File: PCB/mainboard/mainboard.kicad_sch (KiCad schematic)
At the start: 42 parts

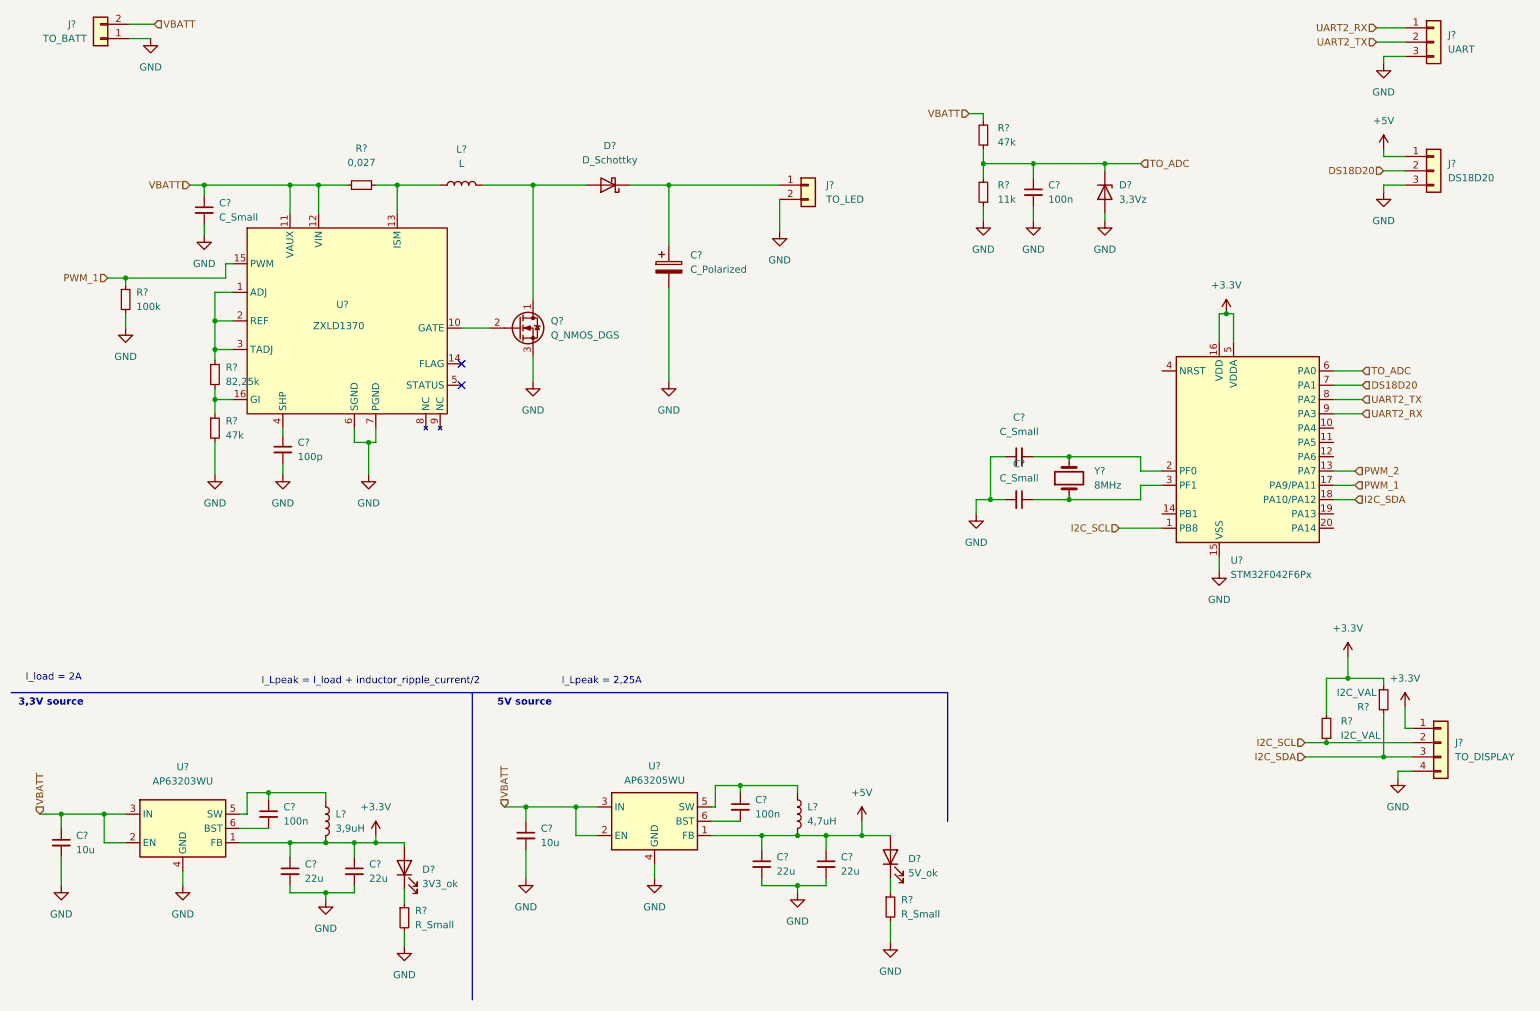
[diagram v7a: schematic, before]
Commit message: Added some calculations, added values to scheme and SWD interface
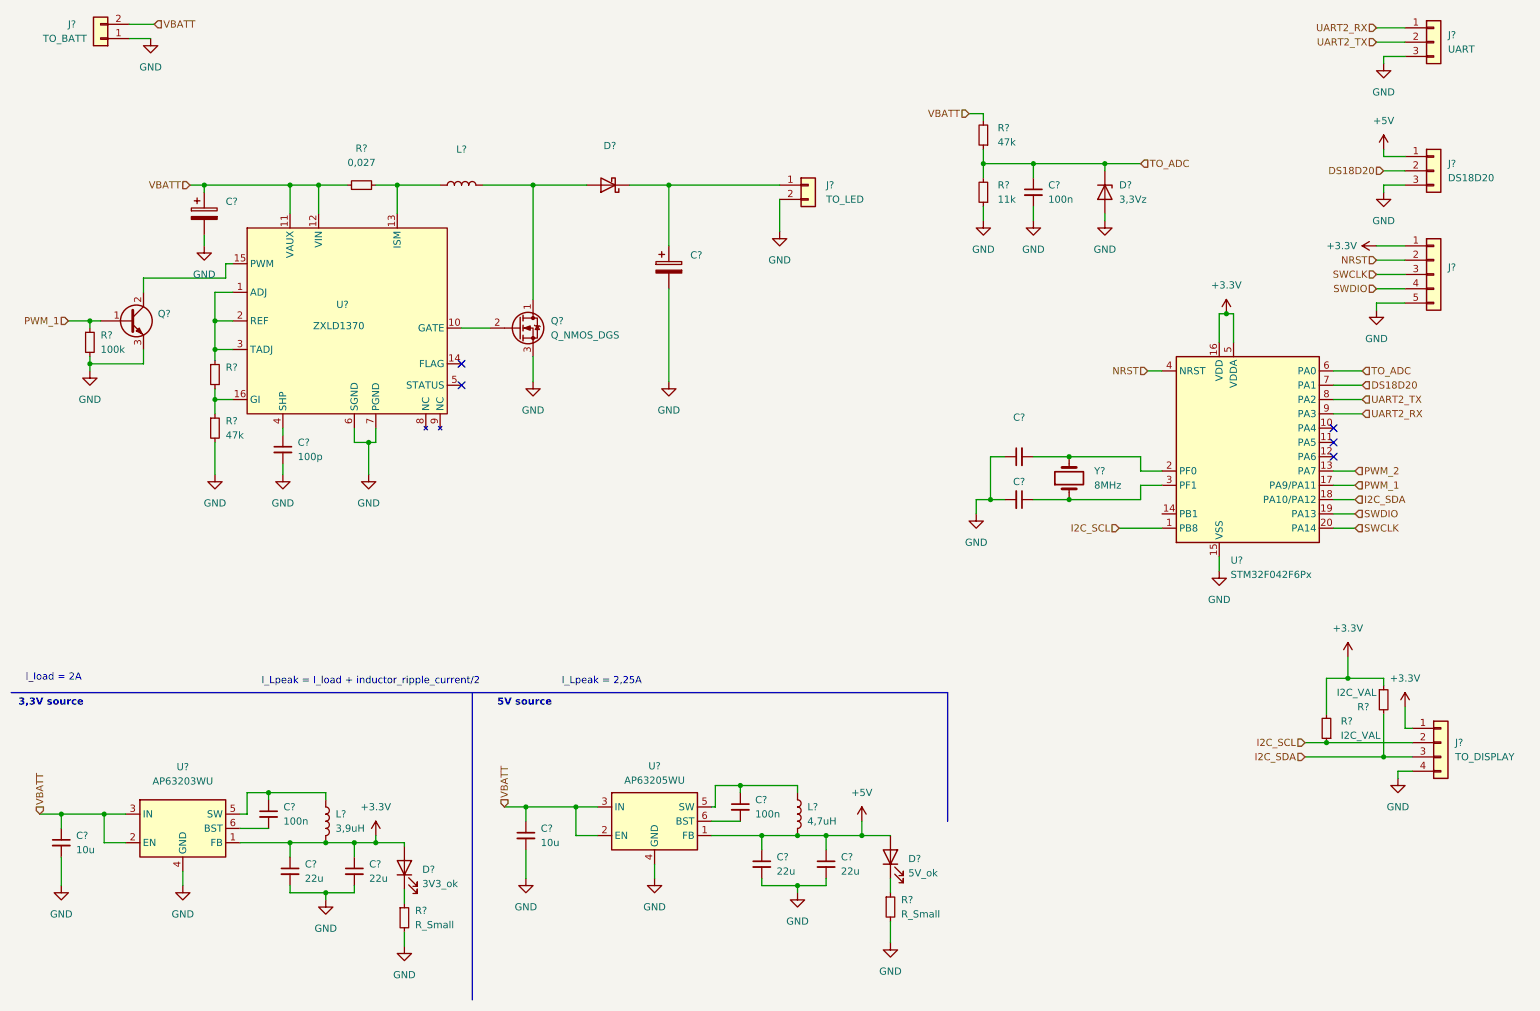
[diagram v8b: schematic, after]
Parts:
- removed C?: C_Small, symbol Device:C_Small
- added C?: (no value), symbol Device:C_Polarized
- added J?: (no value), symbol Connector_Generic:Conn_01x05
- added Q?: (no value), symbol Device:Q_NPN_BCE
- C? (x2): value C_Small -> (none)
- C?: value C_Polarized -> (none)
- D?: value D_Schottky -> (none)
- L?: value L -> (none)
- R?: value 82,25k -> (none)
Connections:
- net +3.3V: now also J?.1 (Pin_1)
- net GND: now also C?.2, J?.5 (Pin_5), Q?.3 (E)
- net PWM_1: now also Q?.1 (B); no longer U?.15 (PWM)
- net VBATT: now also C?.1
- net SWDIO: now reaches U?.19 (PA13)
- net SWDIO: now also J?.4 (Pin_4)
- net SWCLK: now reaches U?.20 (PA14)
- net SWCLK: now also J?.3 (Pin_3)
- net NRST: now reaches U?.4 (NRST)
- net NRST: now also J?.2 (Pin_2)
- new net: Q?.2 (C), U?.15 (PWM)
- no-connect marks 2 -> 5
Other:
- moved on the sheet: R?
